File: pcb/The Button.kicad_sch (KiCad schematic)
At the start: 33 parts, among them J1 Conn_01x02, J2 2169890001, J4 Conn_01x02, J5 Conn_01x05_Pin, J6 Conn_01x03, J7 Conn_01x02, SW8 SW_SPST BOOT, U1 LD1117S33TR_SOT223, U2 STM32C071KBTx, U5 USBLC6-2SC6

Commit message: Updating for fabrication with jlcpcb
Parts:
- removed U1: LD1117S33TR_SOT223, Package_TO_SOT_SMD:SOT-223-3_TabPin2, symbol Regulator_Linear:LD1117S33TR_SOT223
- added U3: STM32L071KBUx, Package_DFN_QFN:QFN-32-1EP_5x5mm_P0.5mm_EP3.45x3.45mm, symbol MCU_ST_STM32L0:STM32L071KBUx
- added U4: AMS1117-3.3, Package_TO_SOT_SMD:SOT-89-3_Handsoldering, symbol Regulator_Linear:AMS1117-3.3
- C3: value 100n -> 100nF; now not fitted
- C4: value 100n -> 100nF
- C7: value 4.7Uf -> 4.7uF; now not fitted
- C9: value 10uF -> 22uF
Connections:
- net BTN_HI: now also U3.18 (PA8)
- net BTN_KEY: now also U3.13 (PA7)
- net BTN_LO: now also U3.19 (PA9)
- net D_N: now also U3.21 (PA11)
- net D_P: now also U3.22 (PA12)
- net GND: now also U3.16 (VSS), U3.31 (VSS), U3.33 (VSS), U3.4 (VSSA), U4.1 (GND)
- net HW_CFG_1: now also U3.6 (PA0)
- net HW_CFG_2: now also U3.7 (PA1)
- net NRST: now also U3.3 (NRST)
- net SWDCLK: now also U3.25 (PA14)
- net SWDIO: now also U3.23 (PA13)
- net USR_LED_1: now also U3.11 (PA5)
- net USR_LED_2: now also U3.12 (PA6)
- net VDDA_5V: now also U4.3 (VI)
- net VDD_3V: now also U3.17 (VDD), U3.24 (VDDIO2), U3.32 (VDD), U3.5 (VDDA), U4.2 (VO)
- net Extra: now reaches J7.1 (Pin_1), U2.9 (PA2)
- net Extra: now also U3.8 (PA2)
- no-connect marks 18 -> 31
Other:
- moved on the sheet: J5

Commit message: Redesigned and rerouted
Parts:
- removed H1, H2: MountingHole, MountingHole:MountingHole_3.2mm_M3, symbol Mechanical:MountingHole
- removed J2: 2169890001, USB:216989-0001_MOL, symbol USB Connector:2169890001
- added C10: 100nF, Capacitor_SMD:C_0805_2012Metric_Pad1.18x1.45mm_HandSolder, symbol Device:C
- added J6: USB-C-TH_MC-710S-Z13, CustomUsb:USB_THT_SIDE_INSERT_14P, symbol USB Connector:MC-710S-Z13
- SW1: renamed from SW8; footprint Button_Switch_SMD:SW_SPST_FSMSM -> Button_Switch_SMD:SW_PUSH_SPST_3X3MM; LCSC (none) -> C5143623
- U2: renamed from U4; footprint Package_TO_SOT_SMD:SOT-89-3_Handsoldering -> Package_TO_SOT_SMD:SOT-89-3
- U4: renamed from U2; now not fitted
- renumbered C8 to C1, C10 to C11, C4 to C2, C9 to C3, C7 to C4, C6 to C5, C3 to C6, C5 to C7, C2 to C8, C1 to C9, D3 to D2, D4 to D3, J4 to J1, J1 to J2, J6 to J3, J7 to J4, JP2 to JP1, JP1 to JP2, R5 to R2, R6 to R3, R10 to R4, R11 to R5, R7 to R6, U3 to U1, U5 to U3
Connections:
- net D_N: now also J6.A7 (DN1), J6.B7 (DN2)
- net D_P: now also J6.A6 (DP1), J6.B6 (DP2)
- net GND: now also D2.1 (K), C10.1, J6.A1 (GND), J6.A12 (GND), J6.B1 (GND), J6.B12 (GND); no longer R6.2
- net USR_LED_2: now also R6.1; no longer D2.2 (A)
- net VDDA_5V: now also J6.A4 (VBUS), J6.A9 (VBUS), J6.B4 (VBUS), J6.B9 (VBUS)
- net at R5.1: now also J6.A5 (CC1)
- net at R4.1: now also J6.B5 (CC2)
- net BTN_KEY_NC: now reaches U1.20 (PA10)
- net BTN_KEY_NC: now also J3.3 (Pin_3), C10.2
- new net: D2.2 (A), R6.2
- no-connect marks 31 -> 28
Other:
- moved on the sheet: D2, R6

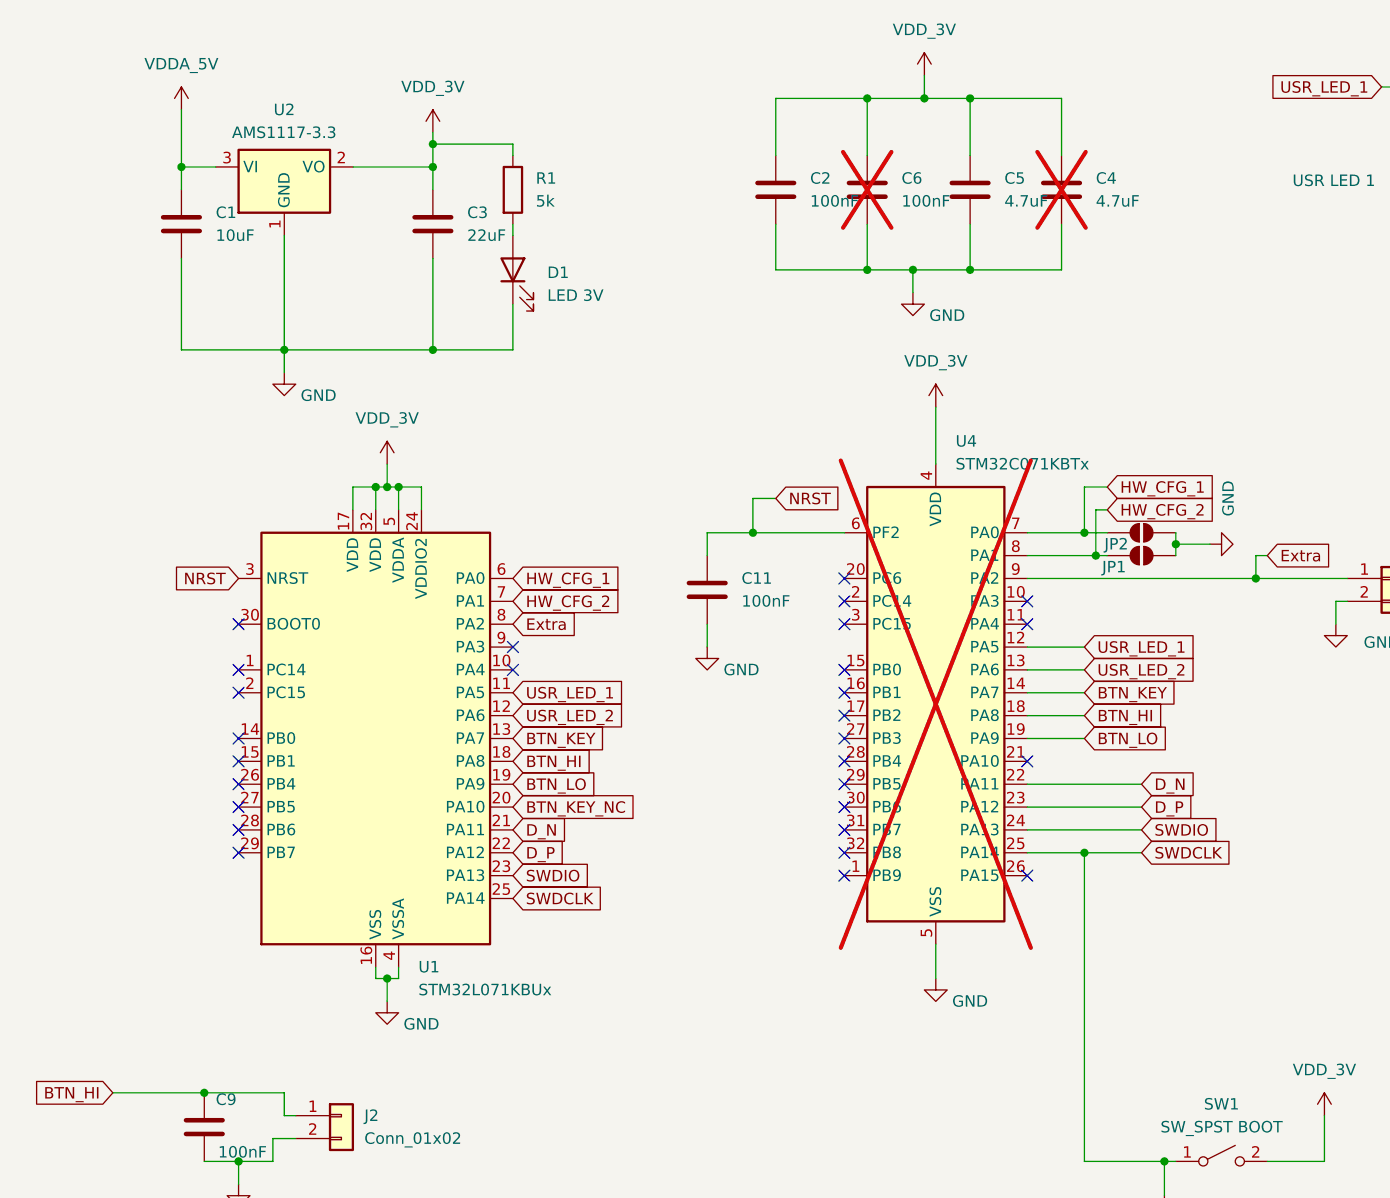
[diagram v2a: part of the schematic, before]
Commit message: Fixed to use correct MCU - STM32*C*071, not L
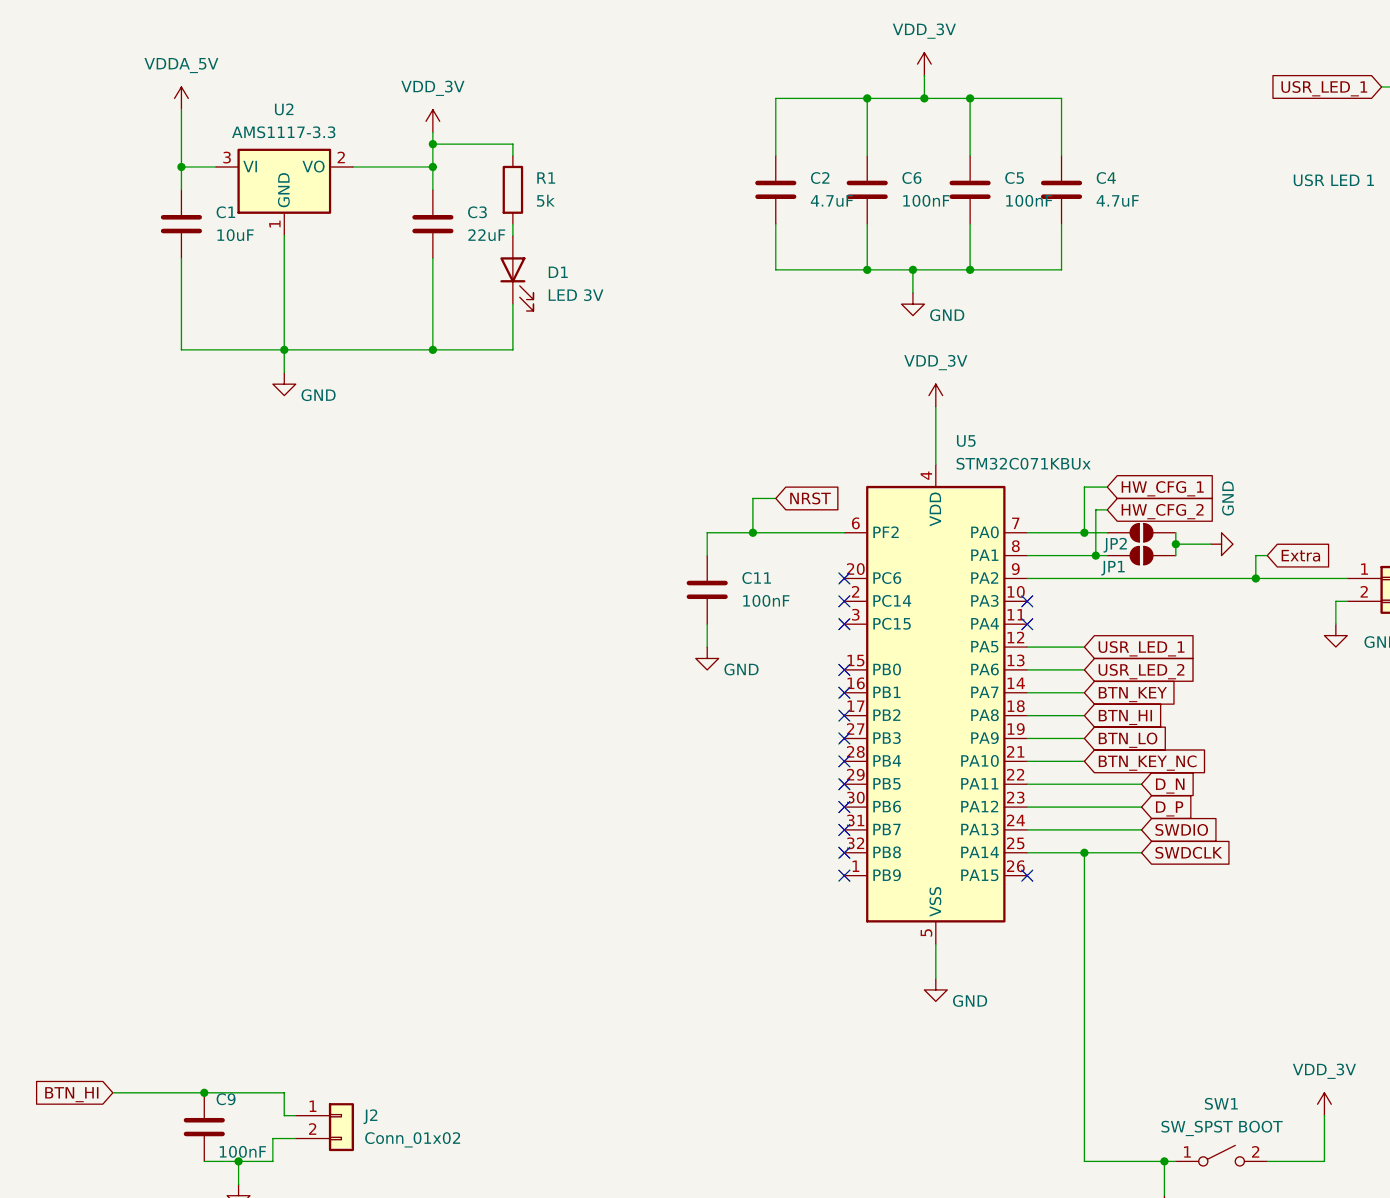
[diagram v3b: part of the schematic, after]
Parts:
- removed U1: STM32L071KBUx, Package_DFN_QFN:QFN-32-1EP_5x5mm_P0.5mm_EP3.45x3.45mm, symbol MCU_ST_STM32L0:STM32L071KBUx
- removed U4: STM32C071KBTx, Package_QFP:LQFP-32_7x7mm_P0.8mm, symbol MCU_ST_STM32C0:STM32C071KBTx
- added U5: STM32C071KBUx, Package_DFN_QFN:QFN-32-1EP_5x5mm_P0.5mm_EP3.45x3.45mm, symbol MCU_ST_STM32C0:STM32C071KBUx
- C2: value 100nF -> 4.7uF
- C4, C6: now fitted
- C5: value 4.7uF -> 100nF
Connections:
- net BTN_HI: now also U5.18 (PA8)
- net BTN_KEY: now also U5.14 (PA7)
- net BTN_KEY_NC: now also U5.21 (PA10)
- net BTN_LO: now also U5.19 (PA9)
- net D_N: now also U5.22 (PA11)
- net D_P: now also U5.23 (PA12)
- net Extra: now also U5.9 (PA2)
- net GND: now also U5.33 (VSS), U5.5 (VSS)
- net HW_CFG_1: now also U5.7 (PA0)
- net HW_CFG_2: now also U5.8 (PA1)
- net NRST: now also U5.6 (PF2)
- net SWDCLK: now also U5.25 (PA14)
- net SWDIO: now also U5.24 (PA13)
- net USR_LED_1: now also U5.12 (PA5)
- net USR_LED_2: now also U5.13 (PA6)
- net VDD_3V: now also U5.4 (VDD)
- no-connect marks 28 -> 16
